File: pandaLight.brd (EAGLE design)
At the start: 100 x 50 mm, 161 parts, among them J1 PJ-037A, U1 MIC23450AAAYML, U10 AS4C128M16D3, U11 PMOD-2X6, U12 PMOD-2X6, U13 PLR135-T10, U14 PLT133-T10W, U15 PLR135-T10, U16 TP10SQ, U17 TP10SQ, U18 PAN1322, U2 6SLX45CSG324, U3 TPD4S014SON, U4 FT2232HL, U5 93LC46BT-I/OT, U6 TPD12S016PWR, U7 TPD12S016PWR, U8 N25Q128AF8, U9 TPD12S016PWR, X1 USBUB-S, X2 HDMI_RECEPTICAL_A, X3 HDMI_RECEPTICAL_A, X4 HDMI_RECEPTICAL_A, Y1 403, Y2 20Mhz

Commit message: First routing of the serial flash; Placed some more bypass capacitors
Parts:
- moved R38 173.1 mm to (74.1, 16.9), turned to 180 degrees
- moved R34 168.0 mm to (74.1, 18.1)
- moved R33 163.1 mm to (74.4, 19.1)
- moved R32 148.9 mm to (62.2, 20.6), turned to 180 degrees
- moved C3 148.5 mm to (44.0, 31.0), turned to 270 degrees
- moved R35 146.0 mm to (62.2, 18.9), turned to 180 degrees
- moved C2 140.0 mm to (41.8, 34.5), turned to 90 degrees
- moved LED2 126.6 mm to (59.2, 16.7), turned to 90 degrees
- moved R36 108.5 mm to (59.2, 15.5), turned to 180 degrees
- moved C5 85.6 mm to (51.0, 26.6), flipped to the bottom
- moved C4 84.2 mm to (55.1, 24.4), flipped to the bottom, turned to 90 degrees
- moved U8 25.2 mm to (68.2, 18.7)
- moved C45 14.0 mm to (64.9, 27.4)
- moved U12 6.86 mm to (142.6, 38.5)
- moved R49 6.16 mm to (82.7, 22.9)
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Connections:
- removed net +5V_SUPPLY: X2.18, X3.18
- net GND: now also U8.ETP
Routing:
- net BT_RESET#: track 2.31 -> 31.1 mm
- net N$46: track 0.00 -> 20.9 mm, vias 0 -> 2
- net N$41: track 0.00 -> 18.8 mm, vias 0 -> 2
- net N$42: track 0.00 -> 18.8 mm, vias 0 -> 2
- net N$40: track 0.00 -> 18.6 mm, vias 0 -> 2
- net GND: track 132.0 -> 145.8 mm, vias 125 -> 152
- net +3V3: track 85.7 -> 96.3 mm, vias 54 -> 70
- net N$44: track 0.00 -> 9.86 mm, vias 0 -> 2
- net N$43: track 0.00 -> 9.61 mm, vias 0 -> 2
- net +1V2: track 12.8 -> 21.0 mm, vias 4 -> 12
- net BT_RX: track 36.0 -> 34.3 mm
- net N$33: track 0.00 -> 1.62 mm
- net N$38: track 0.00 -> 1.24 mm
- net TOS_IN0: track 39.8 -> 39.0 mm

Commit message: Routed HDMI_TX0; Placed the PMODs to the board's bottom left edge
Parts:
- moved C69 163.5 mm to (69.7, 13.3)
- moved U12 136.6 mm to (8.69, 11.4), turned to 0 degrees
- moved JP3 122.5 mm to (18.5, 10.2), turned to 270 degrees
- moved JP2 118.6 mm to (21.8, 10.2), turned to 270 degrees
- moved U11 92.3 mm to (31.6, 11.4), turned to 0 degrees
- moved C58 32.2 mm to (-26.3, 30.3)
- moved C67 32.2 mm to (-20.0, 35.4)
- moved R41 32.2 mm to (-20.0, 25.2)
- moved R42 32.2 mm to (-44.1, 12.5)
- moved R43 32.2 mm to (-39.0, 12.5)
- moved C11 32.2 mm to (-70.8, 35.4)
- moved C12 32.2 mm to (-77.1, 30.3)
- moved C51 32.2 mm to (-60.6, 35.4)
- moved C52 32.2 mm to (-64.4, 30.3)
- moved C53 32.2 mm to (-70.8, 30.3)
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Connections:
- net HDMI_TX0_CEC_3V3: now also U2.V15; no longer U2.N8
- net HDMI_TX0_CTRL_EN: now also U2.V7; no longer U2.U7
- net HDMI_TX0_HPD_3V3: now also U2.V12; no longer U2.M8
- net HDMI_TX0_SCL_3V3: now also U2.U13; no longer U2.R8
- net HDMI_TX0_SDA_3V3: now also U2.V13; no longer U2.T8
- net TOS_OUT0: now also U2.V16; no longer U2.V6
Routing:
- net HDMI_TX0_CTRL_EN: track 0.00 -> 23.5 mm, vias 0 -> 3
- net TOS_OUT0: track 0.00 -> 17.4 mm, vias 0 -> 1
- net HDMI_TX0_SCL_3V3: track 0.00 -> 15.4 mm, vias 0 -> 1
- net HDMI_TX0_HPD_3V3: track 0.00 -> 14.8 mm, vias 0 -> 1
- net HDMI_TX0_CEC_3V3: track 0.00 -> 14.6 mm, vias 0 -> 1
- net HDMI_TX0_SDA_3V3: track 0.00 -> 14.5 mm, vias 0 -> 1
- net GND: track 145.8 -> 160.3 mm, vias 152 -> 163
- net HDMI_TX0_DATA0_P: track 0.00 -> 12.8 mm, vias 0 -> 1
- net HDMI_TX0_CLK_P: track 0.00 -> 12.8 mm, vias 0 -> 1
- net HDMI_TX0_DATA1_P: track 0.00 -> 12.8 mm, vias 0 -> 1
- net HDMI_TX0_DATA2_N: track 0.00 -> 12.8 mm, vias 0 -> 1
- net HDMI_TX0_DATA0_N: track 0.00 -> 12.8 mm, vias 0 -> 1
- net HDMI_TX0_DATA1_N: track 0.00 -> 12.8 mm, vias 0 -> 1
- net HDMI_TX0_CLK_N: track 0.00 -> 12.7 mm, vias 0 -> 1
- net HDMI_TX0_DATA2_P: track 0.00 -> 12.7 mm, vias 0 -> 1
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
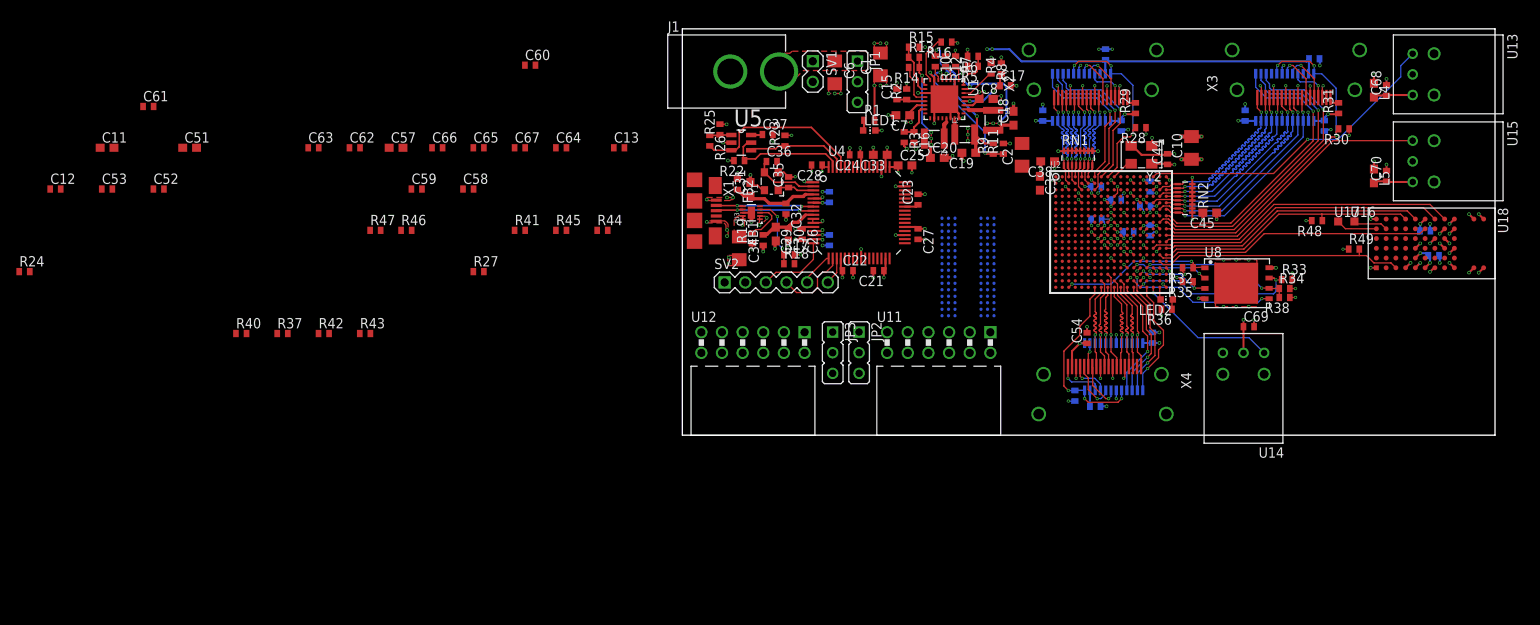
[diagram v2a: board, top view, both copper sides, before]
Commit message: Switched the 1*8 resistor networks with 2*4 ones; Moved the HDMI_RX0 nets to the top layer
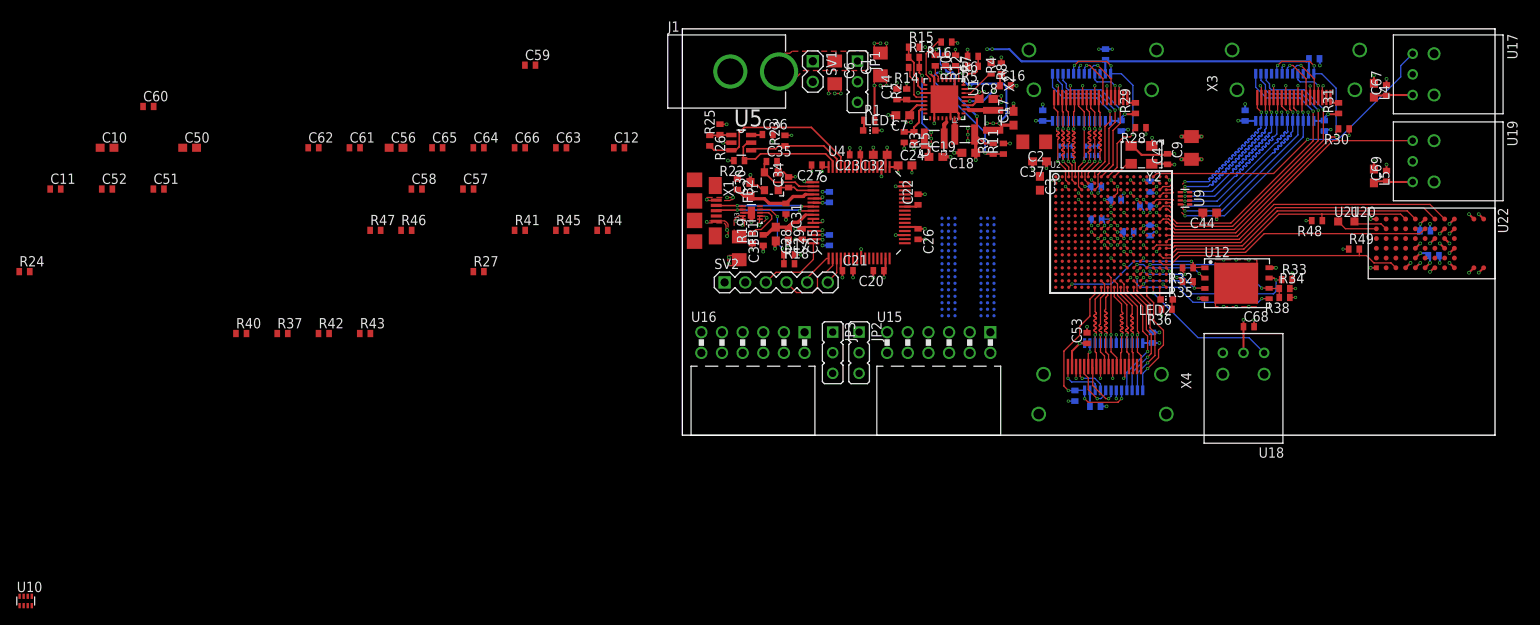
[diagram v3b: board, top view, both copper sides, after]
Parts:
- removed C72: 0.1u, pandaLight:0402
- removed RN1, RN2: MNR18, pandaLight:MNR18
- added C9: 100u, pandaLight:1206
- added U19: PLR135-T10, pandaLight:PLR135-T10_PLT133-T10W
- added U20, U21: TP10SQ, pandaLight:TP10SQ
- added U22: PAN1322, pandaLight:PAN1322
- C10: value 100u -> 4.7u; device pandaLight:1206 -> pandaLight:0603
- C11, C38, C45, C51, C57: value 4.7u -> 0.47u; device pandaLight:0603 -> pandaLight:0402
- C14, C40, C47, C53: value 0.47u -> 0.1u
- C17, C24, C28, C30, C32, C37, C44, C50, C56: value 0.1u -> 4.7u; device pandaLight:0402 -> pandaLight:0603
- C20, C25, C29, C31: value 4.7u -> 0.1u; device pandaLight:0603 -> pandaLight:0402
- C33: value 4.7u -> 100u; device pandaLight:0603 -> pandaLight:1206
- C34: value 100u -> 27p; device pandaLight:1206 -> pandaLight:0402
- C36: value 27p -> 0.1u
- C59: value 0.47u -> 1u
- C61: value 1u -> 0.1u
- U10: value AS4C128M16D3 -> 51; device pandaLight:96-FBGA_13X9 -> pandaLight:741C083
- U11: value PMOD-2X6 -> TPD12S016PWR; device pandaLight:PMOD-2X6 -> pandaLight:PW_R-PDSO-G24
- U12: value PMOD-2X6 -> N25Q128AF8; device pandaLight:PMOD-2X6 -> pandaLight:V-PDFN-8_8X6
- U13: value PLR135-T10 -> TPD12S016PWR; device pandaLight:PLR135-T10_PLT133-T10W -> pandaLight:PW_R-PDSO-G24
- U14: value PLT133-T10W -> AS4C128M16D3; device pandaLight:PLR135-T10_PLT133-T10W -> pandaLight:96-FBGA_13X9
- U15: value PLR135-T10 -> PMOD-2X6; device pandaLight:PLR135-T10_PLT133-T10W -> pandaLight:PMOD-2X6
- U16: value TP10SQ -> PMOD-2X6; device pandaLight:TP10SQ -> pandaLight:PMOD-2X6
- U17: value TP10SQ -> PLR135-T10; device pandaLight:TP10SQ -> pandaLight:PLR135-T10_PLT133-T10W
- U18: value PAN1322 -> PLT133-T10W; device pandaLight:PAN1322 -> pandaLight:PLR135-T10_PLT133-T10W
- U6, U7, U9: value TPD12S016PWR -> 51; device pandaLight:PW_R-PDSO-G24 -> pandaLight:741C083
- U8: value N25Q128AF8 -> TPD12S016PWR; device pandaLight:V-PDFN-8_8X6 -> pandaLight:PW_R-PDSO-G24
- moved C10 133.4 mm to (-70.8, 35.4), turned to 0 degrees
- moved C50 129.9 mm to (-60.6, 35.4), flipped to the top, turned to 0 degrees
- moved U10 123.0 mm to (-80.8, -20.4), flipped to the top, turned to 0 degrees
- moved C53 122.0 mm to (49.8, 11.9), turned to 90 degrees
- moved C67 106.9 mm to (86.7, 42.5), turned to 90 degrees
- moved C56 96.0 mm to (-35.2, 35.4), flipped to the top, turned to 0 degrees
- moved U16 75.5 mm to (8.69, 11.4)
- moved C12 69.5 mm to (-7.78, 35.4)
- moved U15 64.9 mm to (31.6, 11.4), turned to 0 degrees
- moved C13 61.5 mm to (53.4, 28.9), flipped to the bottom, turned to 180 degrees
- moved U12 59.9 mm to (68.2, 18.7)
- moved U13 53.4 mm to (53.1, 8.43), flipped to the bottom, turned to 90 degrees
- moved U11 52.2 mm to (74.1, 41.6), flipped to the bottom, turned to 270 degrees
- moved C60 47.3 mm to (-65.7, 40.5)
- moved U14 36.4 mm to (35.1, 20.7), flipped to the bottom
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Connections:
- net +1V2: now also C19.1; no longer C20.1
- net +1V5: now also C18.1, C56.1, U14.A1, U14.A8, U14.B2, U14.C1, U14.C9, U14.D2, U14.D9, U14.E9, U14.F1, U14.G7, U14.H2, U14.H9, U14.K2, U14.K8, U14.N1, U14.N9, U14.R1, U14.R9; no longer C19.1, C64.1, U10.A1, U10.A8, U10.B2, U10.C1, U10.C9, U10.D2, U10.D9, U10.E9, U10.F1, U10.G7, U10.H2, U10.H9, U10.K2, U10.K8, U10.N1, U10.N9, U10.R1, U10.R9
- net +1V5_VREF: now also C63.2, C64.1, U14.H1, U14.M8; no longer C64.2, C67.1, U10.H1, U10.M8
- net +1V8: now also C24.1; no longer C28.1
- net +3V3: now also C17.1, C20.1, C32.1, C36.1, C42.1, C49.1, C55.1, C68.1, C70.1, C9.1, U10.5, U10.6, U10.7, U10.8, U11.24, U12.8, U13.24, U18.2, U22.A4, U22.A5, U22.A6, U22.B5, U22.C5, U22.F6, U6.5, U6.6, U6.7, U6.8, U7.5, U7.6, U7.7, U7.8, U8.24, U9.5, U9.6, U9.7, U9.8; no longer C14.1, C18.1, C24.1, C33.1, C40.1, C47.1, C53.1, C56.1, C69.1, C72.1, RN1.10, RN1.11, RN1.12, RN1.13, RN1.14, RN1.15, RN1.16, RN1.9, RN2.10, RN2.11, RN2.12, RN2.13, RN2.14, RN2.15, RN2.16, RN2.9, U14.2, U18.A4, U18.A5, U18.A6, U18.B5, U18.C5, U18.F6, U6.24, U7.24, U8.8, U9.24
- net +5V: now also C41.1, C48.1, C54.1, U11.11, U13.11, U8.11; no longer C42.1, C49.1, C55.1, U6.11, U7.11, U9.11
- net BT_CTS: now also U22.F5; no longer U18.F5
- net BT_RESET#: now also U22.A3; no longer U18.A3
- net BT_RTS: now also U22.F8; no longer U18.F8
- net BT_RX: now also U22.E6; no longer U18.E6
- net BT_TX: now also U22.F7; no longer U18.F7
- net BT_WAKE: now also U22.F4; no longer U18.F4
- net DDR3_A0: now also U14.N3; no longer U10.N3
- net DDR3_A1: now also U14.P7; no longer U10.P7
- net DDR3_A10: now also U14.L7; no longer U10.L7
- net DDR3_A11: now also U14.R7; no longer U10.R7
- net DDR3_A12: now also U14.N7; no longer U10.N7
- net DDR3_A2: now also U14.P3; no longer U10.P3
- net DDR3_A3: now also U14.N2; no longer U10.N2
- net DDR3_A4: now also U14.P8; no longer U10.P8
- net DDR3_A5: now also U14.P2; no longer U10.P2
- net DDR3_A6: now also U14.R8; no longer U10.R8
- net DDR3_A7: now also U14.R2; no longer U10.R2
- net DDR3_A8: now also U14.T8; no longer U10.T8
- net DDR3_A9: now also U14.R3; no longer U10.R3
- net DDR3_BA0: now also U14.M2; no longer U10.M2
- net DDR3_BA1: now also U14.N8; no longer U10.N8
- net DDR3_BA2: now also U14.M3; no longer U10.M3
- net DDR3_CAS#: now also U14.K3; no longer U10.K3
- net DDR3_CK: now also U14.J7; no longer U10.J7
- net DDR3_CK#: now also U14.K7; no longer U10.K7
- net DDR3_CKE: now also U14.K9; no longer U10.K9
- net DDR3_DQ0: now also U14.E3; no longer U10.E3
- net DDR3_DQ1: now also U14.F7; no longer U10.F7
- net DDR3_DQ10: now also U14.C8; no longer U10.C8
- net DDR3_DQ11: now also U14.C2; no longer U10.C2
- net DDR3_DQ12: now also U14.A7; no longer U10.A7
- net DDR3_DQ13: now also U14.A2; no longer U10.A2
- net DDR3_DQ14: now also U14.B8; no longer U10.B8
- net DDR3_DQ15: now also U14.A3; no longer U10.A3
- net DDR3_DQ2: now also U14.F2; no longer U10.F2
- net DDR3_DQ3: now also U14.F8; no longer U10.F8
- net DDR3_DQ4: now also U14.H3; no longer U10.H3
- net DDR3_DQ5: now also U14.H8; no longer U10.H8
- net DDR3_DQ6: now also U14.G2; no longer U10.G2
- net DDR3_DQ7: now also U14.H7; no longer U10.H7
- net DDR3_DQ8: now also U14.D7; no longer U10.D7
- net DDR3_DQ9: now also U14.C3; no longer U10.C3
- net DDR3_LDM: now also U14.E7; no longer U10.E7
- net DDR3_LDQS: now also U14.F3; no longer U10.F3
- net DDR3_LDQS#: now also U14.G3; no longer U10.G3
- net DDR3_ODT: now also U14.K1; no longer U10.K1
- net DDR3_RAS#: now also U14.J3; no longer U10.J3
- net DDR3_RESET#: now also U14.T2; no longer U10.T2
- net DDR3_UDM: now also U14.D3; no longer U10.D3
- net DDR3_UDQS: now also U14.C7; no longer U10.C7
- net DDR3_UDQS#: now also U14.B7; no longer U10.B7
- net DDR3_WE#: now also U14.L3; no longer U10.L3
- net GND: now also C64.2, C9.2, U11.14, U11.19, U11.6, U12.4, U12.ETP, U13.14, U13.19, U13.6, U14.A9, U14.B1, U14.B3, U14.B9, U14.D1, U14.D8, U14.E1, U14.E2, U14.E8, U14.F9, U14.G1, U14.G8, U14.G9, U14.J2, U14.J8, U14.L2, U14.M1, U14.M9, U14.P1, U14.P9, U14.T1, U14.T9, U15.11, U15.5, U16.11, U16.5, U17.2, U18.1, U19.2, U22.A1, U22.A11, U22.A12, U22.A7, U22.A9, U22.C8, U22.C9, U22.D7, U22.D8, U22.E8, U22.E9, U22.F1, U22.F11, U22.F12, U22.F9, U8.14, U8.19, U8.6; no longer C63.2, C72.2, U10.A9, U10.B1, U10.B3, U10.B9, U10.D1, U10.D8, U10.E1, U10.E2, U10.E8, U10.F9, U10.G1, U10.G8, U10.G9, U10.J2, U10.J8, U10.L2, U10.M1, U10.M9, U10.P1, U10.P9, U10.T1, U10.T9, U11.11, U11.5, U12.11, U12.5, U13.2, U14.1, U15.2, U18.A1, U18.A11, U18.A12, U18.A7, U18.A9, U18.C8, U18.C9, U18.D7, U18.D8, U18.E8, U18.E9, U18.F1, U18.F11, U18.F12, U18.F9, U6.14, U6.19, U6.6, U7.14, U7.19, U7.6, U8.4, U8.ETP, U9.14, U9.19, U9.6
- net HDMI_RX0_5V: now also C40.1, U8.13; no longer C41.1, U6.13
- net HDMI_RX0_CEC: now also U8.7; no longer U6.7
- net HDMI_RX0_CEC_3V3: now also U8.1; no longer U6.1
- net HDMI_RX0_CLK_N: now also U7.1, U8.15; no longer RN1.8, U6.15
- net HDMI_RX0_CLK_P: now also U7.2, U8.16; no longer RN1.7, U6.16
- net HDMI_RX0_CTRL_EN: now also U8.12, U8.5; no longer U6.12, U6.5
- net HDMI_RX0_DATA0_N: now also U7.3, U8.17; no longer RN1.6, U6.17
- net HDMI_RX0_DATA0_P: now also U7.4, U8.18; no longer RN1.5, U6.18
- net HDMI_RX0_DATA1_N: now also U6.1, U8.20; no longer RN1.4, U6.20
- net HDMI_RX0_DATA1_P: now also U6.2, U8.21; no longer RN1.3, U6.21
- net HDMI_RX0_DATA2_N: now also U6.3, U8.22; no longer RN1.2, U6.22
- net HDMI_RX0_DATA2_P: now also U6.4, U8.23; no longer RN1.1, U6.23
- net HDMI_RX0_SCL_3V3: now also U8.2; no longer U6.2
- net HDMI_RX0_SCL_5V: now also U8.8; no longer U6.8
- net HDMI_RX0_SDA_3V3: now also U8.3; no longer U6.3
- net HDMI_RX0_SDA_5V: now also U8.9; no longer U6.9
- net HDMI_RX1_5V: now also C47.1, U11.13; no longer C48.1, U7.13
- net HDMI_RX1_CEC: now also U11.7; no longer U7.7
- net HDMI_RX1_CEC_3V3: now also U11.1; no longer U7.1
- net HDMI_RX1_CLK_N: now also U10.1, U11.15; no longer RN2.8, U7.15
- net HDMI_RX1_CLK_P: now also U10.2, U11.16; no longer RN2.7, U7.16
- net HDMI_RX1_CTRL_EN: now also U11.12, U11.5; no longer U7.12, U7.5
- net HDMI_RX1_DATA0_N: now also U10.3, U11.17; no longer RN2.6, U7.17
- net HDMI_RX1_DATA0_P: now also U10.4, U11.18; no longer RN2.5, U7.18
- net HDMI_RX1_DATA1_N: now also U11.20, U9.1; no longer RN2.4, U7.20
- net HDMI_RX1_DATA1_P: now also U11.21, U9.2; no longer RN2.3, U7.21
- net HDMI_RX1_DATA2_N: now also U11.22, U9.3; no longer RN2.2, U7.22
- net HDMI_RX1_DATA2_P: now also U11.23, U9.4; no longer RN2.1, U7.23
- net HDMI_RX1_SCL_3V3: now also U11.2; no longer U7.2
- net HDMI_RX1_SCL_5V: now also U11.8; no longer U7.8
- net HDMI_RX1_SDA_3V3: now also U11.3; no longer U7.3
- net HDMI_RX1_SDA_5V: now also U11.9; no longer U7.9
- net HDMI_TX0_5V: now also C53.1, U13.13; no longer C54.1, U9.13
- net HDMI_TX0_CEC: now also U13.7; no longer U9.7
- net HDMI_TX0_CEC_3V3: now also U13.1; no longer U9.1
- net HDMI_TX0_CLK_N: now also U13.15; no longer U9.15
- net HDMI_TX0_CLK_P: now also U13.16; no longer U9.16
- net HDMI_TX0_CTRL_EN: now also U13.12, U13.5; no longer U9.12, U9.5
- net HDMI_TX0_DATA0_N: now also U13.17; no longer U9.17
- net HDMI_TX0_DATA0_P: now also U13.18; no longer U9.18
- net HDMI_TX0_DATA1_N: now also U13.20; no longer U9.20
- net HDMI_TX0_DATA1_P: now also U13.21; no longer U9.21
- net HDMI_TX0_DATA2_N: now also U13.22; no longer U9.22
- net HDMI_TX0_DATA2_P: now also U13.23; no longer U9.23
- net HDMI_TX0_HPD_3V3: now also U13.4; no longer U9.4
- net HDMI_TX0_HPD_5V: now also U13.10; no longer U9.10
- net HDMI_TX0_SCL_3V3: now also U13.2; no longer U9.2
- net HDMI_TX0_SCL_5V: now also U13.8; no longer U9.8
- net HDMI_TX0_SDA_3V3: now also U13.3; no longer U9.3
- net HDMI_TX0_SDA_5V: now also U13.9; no longer U9.9
- net N$1: now also C35.1; no longer C36.1
- net N$15: now also C16.1; no longer C17.1
- net N$19: now also U21.TP, U22.E1; no longer U17.TP, U18.E1
- net N$28: now also C30.1; no longer C32.1
- net N$29: now also U20.TP, U22.E2; no longer U16.TP, U18.E2
- net N$3: now also U14.L8; no longer U10.L8
- net N$30: now also C15.1; no longer C16.1
- net N$31: now also C28.1; no longer C30.1
- net N$36: now also C67.1, U17.1; no longer C68.1, U13.1
- net N$4: now also C69.1, U19.1; no longer C70.1, U15.1
- net N$40: now also U12.5; no longer U8.5
- net N$41: now also U12.1; no longer U8.1
- net N$42: now also U12.6; no longer U8.6
- net N$43: now also U12.2; no longer U8.2
- net N$44: now also U12.3; no longer U8.3
- net N$45: now also C33.1; no longer C34.1
- net N$46: now also U12.7; no longer U8.7
- net N$48: now also C14.1; no longer C15.1
- net N$49: now also U16.12, U16.6; no longer U12.12, U12.6
- net N$5: now also C34.1; no longer C35.1
- net N$51: now also U15.12, U15.6; no longer U11.12, U11.6
- net PMOD0_0: now also U15.1; no longer U11.1
- net PMOD0_1: now also U15.2; no longer U11.2
- net PMOD0_2: now also U15.3; no longer U11.3
- net PMOD0_3: now also U15.4; no longer U11.4
- net PMOD1_0: now also U15.7; no longer U11.7
- net PMOD1_1: now also U15.8; no longer U11.8
- net PMOD1_2: now also U15.9; no longer U11.9
- net PMOD1_3: now also U15.10; no longer U11.10
- net PMOD2_0: now also U16.1; no longer U12.1
- net PMOD2_1: now also U16.2; no longer U12.2
- net PMOD2_2: now also U16.3; no longer U12.3
- net PMOD2_3: now also U16.4; no longer U12.4
- net PMOD3_0: now also U16.7; no longer U12.7
- net PMOD3_1: now also U16.8; no longer U12.8
- net PMOD3_2: now also U16.9; no longer U12.9
- net PMOD3_3: now also U16.10; no longer U12.10
- net TOS_IN0: now also U17.3; no longer U13.3
- net TOS_IN1: now also U19.3; no longer U15.3
- net TOS_OUT0: now also U18.3; no longer U14.3
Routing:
- net +3V3: track 102.5 -> 95.4 mm, vias 72 -> 68
- net GND: track 160.3 -> 158.0 mm, vias 163 -> 161
- net HDMI_RX1_DATA1_N: track 26.4 -> 24.1 mm
- net HDMI_RX0_DATA0_P: track 12.1 -> 13.9 mm
- net HDMI_RX0_DATA2_P: track 12.1 -> 13.8 mm
- net HDMI_RX0_CLK_N: track 12.1 -> 13.8 mm
- net HDMI_RX0_CLK_P: track 12.2 -> 13.8 mm
- net HDMI_RX0_DATA1_P: track 12.1 -> 13.8 mm
- net HDMI_RX0_DATA2_N: track 12.1 -> 13.8 mm
- net HDMI_RX0_DATA0_N: track 12.1 -> 13.8 mm
- net HDMI_RX0_DATA1_N: track 12.2 -> 13.8 mm
- net HDMI_RX1_CLK_N: track 26.1 -> 24.8 mm
- net HDMI_RX1_DATA2_P: track 26.3 -> 25.0 mm
- net HDMI_RX1_DATA2_N: track 26.4 -> 25.1 mm
- net HDMI_RX1_DATA1_P: track 26.1 -> 24.8 mm
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
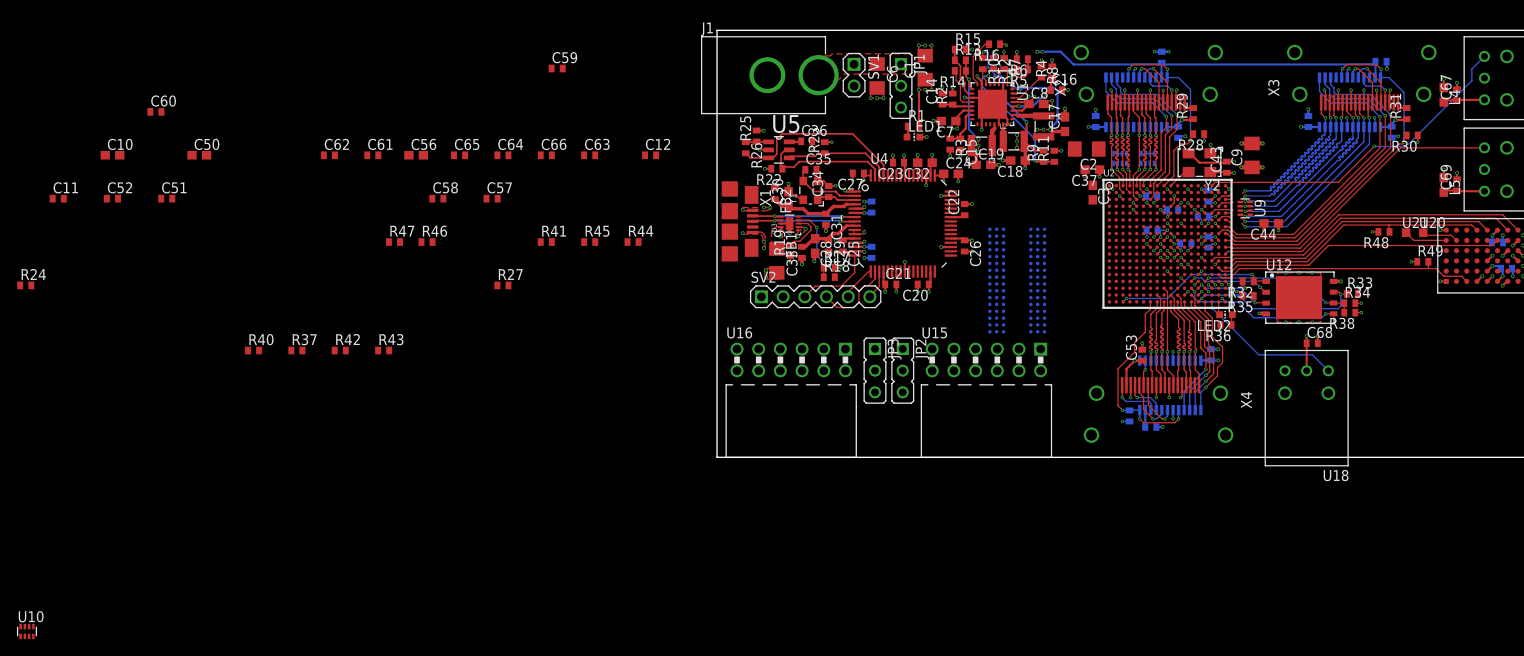
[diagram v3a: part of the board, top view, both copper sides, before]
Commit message: Finished moving the HDMI_RX0 traces to the top layer; Began doing the same with the HDMI_RX1 traces
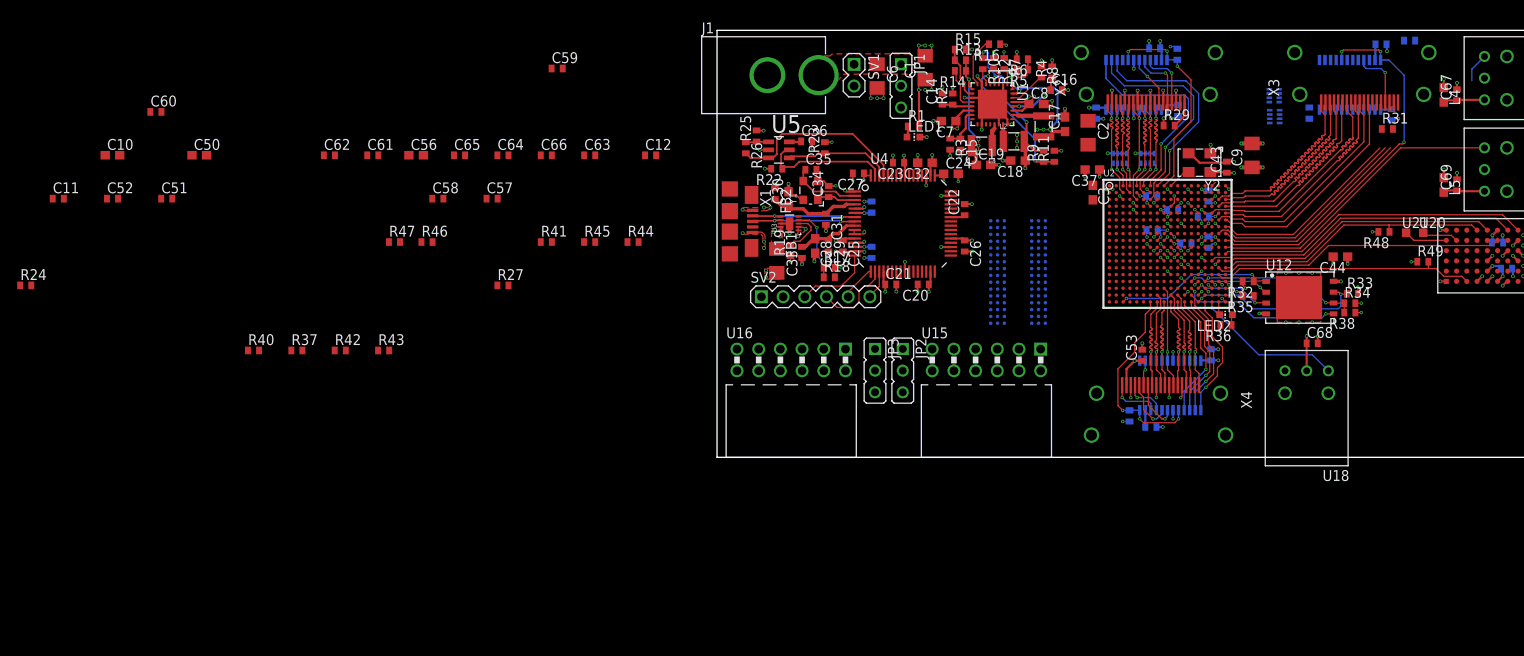
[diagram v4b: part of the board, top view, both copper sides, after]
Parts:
- moved U10 158.1 mm to (65.3, 39.9), flipped to the bottom, turned to 90 degrees
- moved U9 13.6 mm to (65.2, 42.4), flipped to the bottom, turned to 90 degrees
- moved R30 11.1 mm to (81.1, 48.8), flipped to the bottom
- moved R28 9.68 mm to (53.9, 47.2), flipped to the bottom, turned to 270 degrees
- moved C44 8.99 mm to (73.0, 23.5)
- moved R29 3.13 mm to (53.0, 38.9), turned to 0 degrees
- moved R31 2.88 mm to (78.5, 38.5), turned to 0 degrees
- moved C40 2.55 mm to (54.0, 40.6)
- moved C47 2.05 mm to (79.0, 40.1)
- moved C48 2.05 mm to (77.8, 48.4)
- moved U11 2.05 mm to (74.1, 43.6)
- moved U8 2.05 mm to (49.1, 43.6)
- moved C2 1.91 mm to (43.5, 38.0), turned to 270 degrees
- moved C41 1.34 mm to (51.2, 47.9), turned to 0 degrees
- moved U14 1.00 mm to (35.2, 21.7)
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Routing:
- net +5V: track 61.2 -> 21.3 mm, vias 14 -> 13
- net TOS_IN0: track 39.0 -> 4.01 mm, vias 1 -> 0
- net GND: track 158.0 -> 144.4 mm, vias 161 -> 150
- net HDMI_RX1_CEC_3V3: track 36.2 -> 22.6 mm, vias 1 -> 0
- net HDMI_RX1_SCL_3V3: track 37.9 -> 24.4 mm, vias 1 -> 0
- net HDMI_RX1_SDA_3V3: track 37.7 -> 24.2 mm, vias 1 -> 0
- net HDMI_RX1_SCL_5V: track 6.37 -> 0.00 mm, vias 1 -> 0
- net HDMI_RX1_CEC: track 6.15 -> 0.00 mm, vias 1 -> 0
- net HDMI_RX0_CEC_3V3: track 18.8 -> 24.8 mm
- net HDMI_RX0_SCL_3V3: track 20.6 -> 26.4 mm
- net HDMI_RX0_SDA_3V3: track 19.1 -> 24.9 mm
- net HDMI_RX1_DATA1_N: track 24.1 -> 26.8 mm, vias 2 -> 0
- net HDMI_RX1_5V: track 3.62 -> 1.32 mm, vias 1 -> 0
- net HDMI_RX1_SDA_5V: track 4.99 -> 7.04 mm
- net HDMI_RX0_SDA_5V: track 4.99 -> 7.01 mm
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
